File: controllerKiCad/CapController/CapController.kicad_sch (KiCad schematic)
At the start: 1 part

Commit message: Controller PCB Update
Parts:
- removed U?: Arduino_Nano, Arduino:Arduino_Nano, symbol Arduino:Arduino_Nano
- added 7_Seg_Dis_1, 7_Seg_Dis_2, 7_Seg_Dis_3: LTS-6960HR, Display_7Segment:7SegmentLED_LTS6760_LTS6780, symbol Display_Character:LTS-6960HR
- added Nano_33_IoT1: Arduino_Nano_33_IoT_Socket, arduino-library:Arduino_Nano_33_IoT_Socket, symbol arduino-library:Arduino_Nano_33_IoT_Socket
- added PMOD_Connector1: Conn_02x06_Counter_Clockwise, Connector_IDC:IDC-Header_2x06_P2.54mm_Horizontal, symbol Connector_Generic:Conn_02x06_Counter_Clockwise
- added Power_Terminal1: Screw_1x2, TerminalBlock:TerminalBlock_Altech_AK300-2_P5.00mm, symbol Connector:Screw_Terminal_01x02
- added SW_Car1, SW_Car2, SW_Car3, SW_Start1, SW_Stop_Reset1: SW_MEC_5E, symbol Switch:SW_MEC_5E
- added Shift_Reg_1, Shift_Reg_2, Shift_Reg_3: 74LS595, symbol 74xx:74LS595
- added Trigger_Pot1, Wheel_Pot1: Screw_1x3, TerminalBlock:TerminalBlock_Altech_AK300-3_P5.00mm, symbol Connector:Screw_Terminal_01x03
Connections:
- new net: Nano_33_IoT1.D8, Wheel_Pot1.2 (Pin_2)
- new net: Nano_33_IoT1.D13 (D13_SCK), SW_Car3.1
- new net: Nano_33_IoT1.D12 (D12_MISO), SW_Car2.1
- new net: Nano_33_IoT1.VIN, Power_Terminal1.2 (Pin_2)
- new net: 7_Seg_Dis_3.1 (e), Shift_Reg_3.4 (QE)
- new net: 7_Seg_Dis_3.10 (g), Shift_Reg_3.6 (QG)
- new net: 7_Seg_Dis_3.2 (d), Shift_Reg_3.3 (QD)
- new net: 7_Seg_Dis_3.4 (c), Shift_Reg_3.2 (QC)
- new net: 7_Seg_Dis_3.6 (b), Shift_Reg_3.1 (QB)
- new net: 7_Seg_Dis_3.7 (a), Shift_Reg_3.15 (QA)
- new net: 7_Seg_Dis_3.9 (f), Shift_Reg_3.5 (QF)
- new net: Nano_33_IoT1.D10, SW_Start1.1
- new net: 7_Seg_Dis_2.1 (e), Shift_Reg_2.4 (QE)
- new net: 7_Seg_Dis_2.10 (g), Shift_Reg_2.6 (QG)
- new net: 7_Seg_Dis_2.2 (d), Shift_Reg_2.3 (QD)
- new net: 7_Seg_Dis_2.4 (c), Shift_Reg_2.2 (QC)
- new net: 7_Seg_Dis_2.6 (b), Shift_Reg_2.1 (QB)
- new net: 7_Seg_Dis_2.7 (a), Shift_Reg_2.15 (QA)
- new net: 7_Seg_Dis_2.9 (f), Shift_Reg_2.5 (QF)
- new net: Nano_33_IoT1.A3, PMOD_Connector1.10 (Pin_10)
- new net: Nano_33_IoT1.A4 (A4/SDA), PMOD_Connector1.3 (Pin_3)
- new net: Nano_33_IoT1.A5 (A5/SCL), PMOD_Connector1.4 (Pin_4)
- new net: Nano_33_IoT1.A6, PMOD_Connector1.5 (Pin_5)
- new net: Nano_33_IoT1.A7, PMOD_Connector1.6 (Pin_6)
- new net: Nano_33_IoT1.A0 (A0/DAC), PMOD_Connector1.7 (Pin_7)
- new net: Nano_33_IoT1.A1, PMOD_Connector1.8 (Pin_8)
- new net: Nano_33_IoT1.A2, PMOD_Connector1.9 (Pin_9)
- new net: Shift_Reg_1.7 (QH), Shift_Reg_2.14 (SER)
- new net: Shift_Reg_2.7 (QH), Shift_Reg_3.14 (SER)
- new net: Nano_33_IoT1.D11 (D11_MOSI), SW_Car1.1
- new net: Nano_33_IoT1.D7, Trigger_Pot1.2 (Pin_2)
- new net: Nano_33_IoT1.D9, SW_Stop_Reset1.1
- new net: 7_Seg_Dis_1.6 (b), Shift_Reg_1.1 (QB)
- new net: 7_Seg_Dis_1.7 (a), Shift_Reg_1.15 (QA)
- new net: 7_Seg_Dis_1.4 (c), Shift_Reg_1.2 (QC)
- new net: 7_Seg_Dis_1.2 (d), Shift_Reg_1.3 (QD)
- new net: 7_Seg_Dis_1.1 (e), Shift_Reg_1.4 (QE)
- new net: 7_Seg_Dis_1.9 (f), Shift_Reg_1.5 (QF)
- new net: 7_Seg_Dis_1.10 (g), Shift_Reg_1.6 (QG)
- new net +5V: Nano_33_IoT1.3V3 (3.3V), PMOD_Connector1.1 (Pin_1), PMOD_Connector1.12 (Pin_12), Shift_Reg_1.10 (~{SRCLR}), Shift_Reg_1.16 (VCC), Shift_Reg_2.10 (~{SRCLR}), Shift_Reg_2.16 (VCC), Shift_Reg_3.10 (~{SRCLR}), Shift_Reg_3.16 (VCC), Trigger_Pot1.1 (Pin_1), Wheel_Pot1.1 (Pin_1)
- new net GND: 7_Seg_Dis_1.3 (C.A.), 7_Seg_Dis_1.8 (C.A.), 7_Seg_Dis_2.3 (C.A.), 7_Seg_Dis_2.8 (C.A.), 7_Seg_Dis_3.3 (C.A.), 7_Seg_Dis_3.8 (C.A.), Nano_33_IoT1.GND1 (GND), PMOD_Connector1.11 (Pin_11), PMOD_Connector1.2 (Pin_2), Power_Terminal1.1 (Pin_1), SW_Car1.4 (A), SW_Car2.4 (A), SW_Car3.4 (A), SW_Start1.4 (A), SW_Stop_Reset1.4 (A), Shift_Reg_1.13 (~{OE}), Shift_Reg_1.8 (GND), Shift_Reg_2.13 (~{OE}), Shift_Reg_2.8 (GND), Shift_Reg_3.13 (~{OE}), Shift_Reg_3.8 (GND), Trigger_Pot1.3 (Pin_3), Wheel_Pot1.3 (Pin_3)
- new net LED_Data_In: Nano_33_IoT1.D4, Shift_Reg_1.14 (SER)
- new net LED_Data_In_CLK: Nano_33_IoT1.D5, Shift_Reg_1.11 (SRCLK), Shift_Reg_2.11 (SRCLK), Shift_Reg_3.12 (RCLK)
- new net LED_Store_CLK: Nano_33_IoT1.D6, Shift_Reg_1.12 (RCLK)
- no-connect marks 0 -> 7
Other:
- removed sheet 7seg3

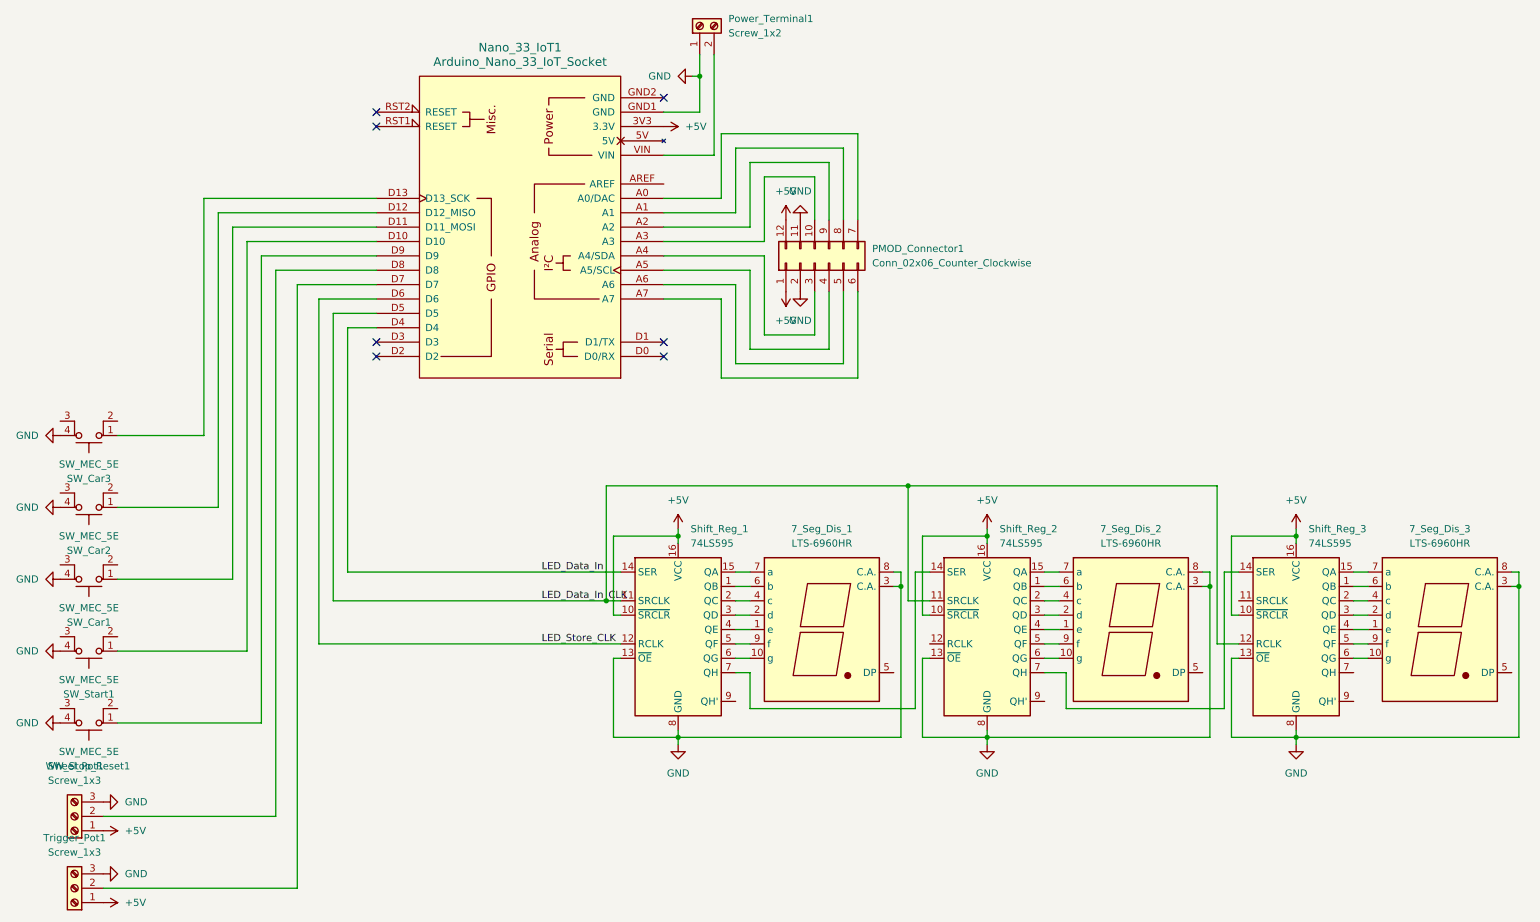
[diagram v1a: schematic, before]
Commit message: finished controller and added legacy veh code
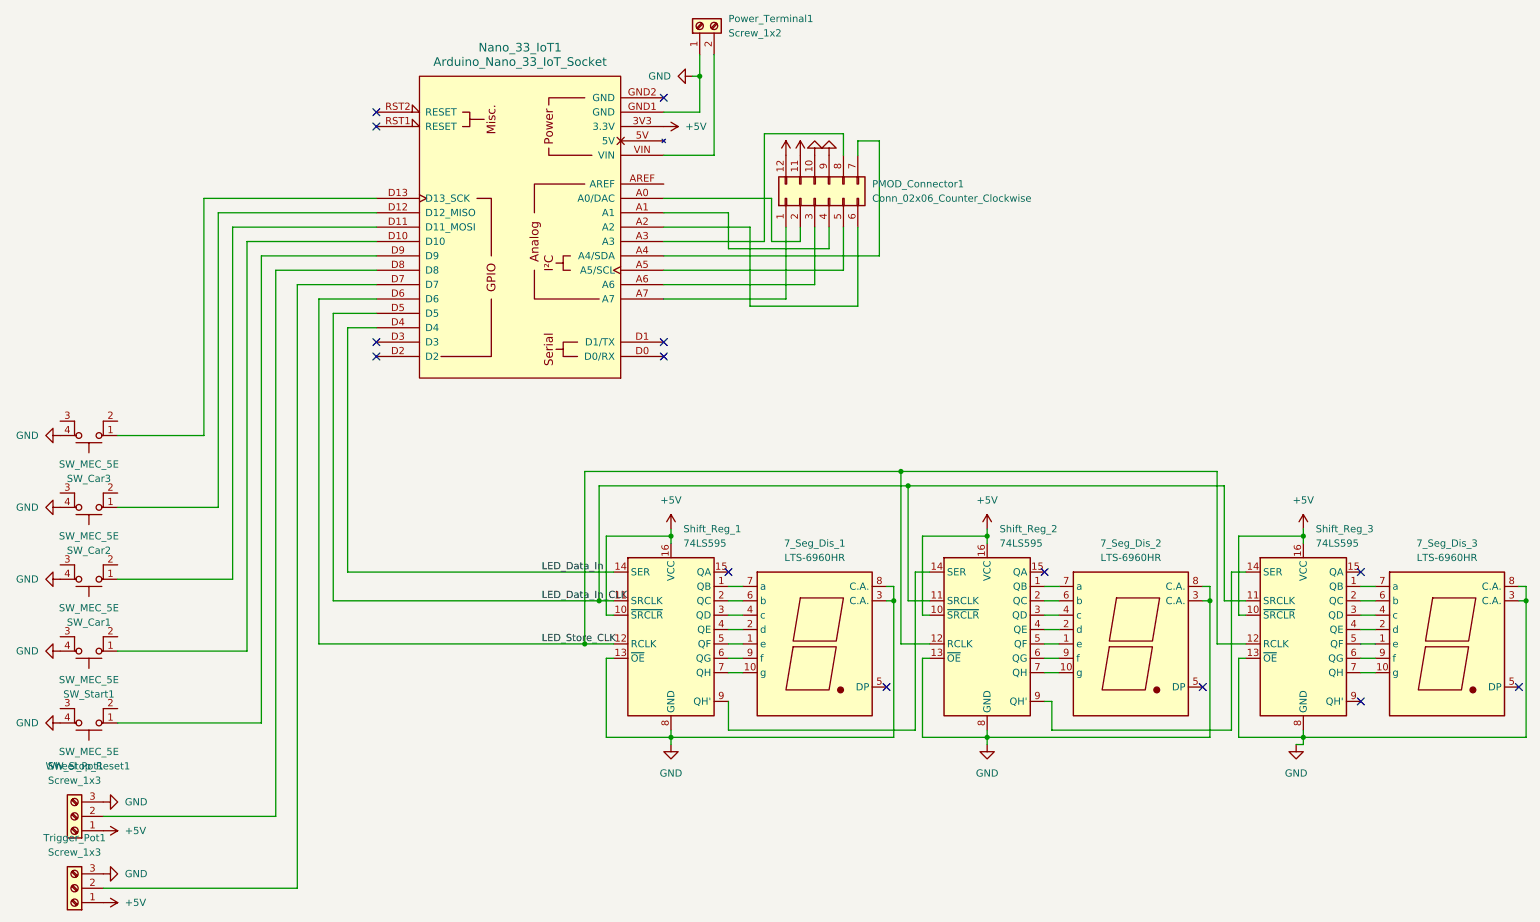
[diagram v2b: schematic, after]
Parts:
- SW_Car1, SW_Car2, SW_Car3, SW_Start1, SW_Stop_Reset1: footprint (none) -> Capstone:4Pin_Button
- Shift_Reg_1, Shift_Reg_2, Shift_Reg_3: footprint (none) -> Capstone:74HC595_16Pin_DIP
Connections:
- net +5V: now also PMOD_Connector1.11 (Pin_11); no longer PMOD_Connector1.1 (Pin_1)
- net GND: now also PMOD_Connector1.10 (Pin_10), PMOD_Connector1.9 (Pin_9); no longer PMOD_Connector1.11 (Pin_11), PMOD_Connector1.2 (Pin_2)
- net LED_Data_In_CLK: now also Shift_Reg_3.11 (SRCLK); no longer Shift_Reg_3.12 (RCLK)
- net LED_Store_CLK: now also Shift_Reg_2.12 (RCLK), Shift_Reg_3.12 (RCLK)
- net at 7_Seg_Dis_3.1 (e): now also Shift_Reg_3.5 (QF); no longer Shift_Reg_3.4 (QE)
- net at 7_Seg_Dis_3.10 (g): now also Shift_Reg_3.7 (QH); no longer Shift_Reg_3.6 (QG)
- net at 7_Seg_Dis_3.2 (d): now also Shift_Reg_3.4 (QE); no longer Shift_Reg_3.3 (QD)
- net at 7_Seg_Dis_3.4 (c): now also Shift_Reg_3.3 (QD); no longer Shift_Reg_3.2 (QC)
- net at 7_Seg_Dis_3.6 (b): now also Shift_Reg_3.2 (QC); no longer Shift_Reg_3.1 (QB)
- net at 7_Seg_Dis_3.7 (a): now also Shift_Reg_3.1 (QB); no longer Shift_Reg_3.15 (QA)
- net at 7_Seg_Dis_3.9 (f): now also Shift_Reg_3.6 (QG); no longer Shift_Reg_3.5 (QF)
- net at 7_Seg_Dis_2.1 (e): now also Shift_Reg_2.5 (QF); no longer Shift_Reg_2.4 (QE)
- net at 7_Seg_Dis_2.10 (g): now also Shift_Reg_2.7 (QH); no longer Shift_Reg_2.6 (QG)
- net at 7_Seg_Dis_2.2 (d): now also Shift_Reg_2.4 (QE); no longer Shift_Reg_2.3 (QD)
- net at 7_Seg_Dis_2.4 (c): now also Shift_Reg_2.3 (QD); no longer Shift_Reg_2.2 (QC)
- net at 7_Seg_Dis_2.6 (b): now also Shift_Reg_2.2 (QC); no longer Shift_Reg_2.1 (QB)
- net at 7_Seg_Dis_2.7 (a): now also Shift_Reg_2.1 (QB); no longer Shift_Reg_2.15 (QA)
- net at 7_Seg_Dis_2.9 (f): now also Shift_Reg_2.6 (QG); no longer Shift_Reg_2.5 (QF)
- net at Nano_33_IoT1.A3: now also PMOD_Connector1.8 (Pin_8); no longer PMOD_Connector1.10 (Pin_10)
- net at PMOD_Connector1.3 (Pin_3): now also Nano_33_IoT1.A6; no longer Nano_33_IoT1.A4 (A4/SDA)
- net at PMOD_Connector1.4 (Pin_4): now also Nano_33_IoT1.A1; no longer Nano_33_IoT1.A5 (A5/SCL)
- net at PMOD_Connector1.5 (Pin_5): now also Nano_33_IoT1.A5 (A5/SCL); no longer Nano_33_IoT1.A6
- net at Nano_33_IoT1.A7: now also PMOD_Connector1.1 (Pin_1); no longer PMOD_Connector1.6 (Pin_6)
- net at Nano_33_IoT1.A0 (A0/DAC): now also PMOD_Connector1.2 (Pin_2); no longer PMOD_Connector1.7 (Pin_7)
- net at Nano_33_IoT1.A2: now also PMOD_Connector1.6 (Pin_6); no longer PMOD_Connector1.9 (Pin_9)
- net at Shift_Reg_2.14 (SER): now also Shift_Reg_1.9 (QH'); no longer Shift_Reg_1.7 (QH)
- net at Shift_Reg_3.14 (SER): now also Shift_Reg_2.9 (QH'); no longer Shift_Reg_2.7 (QH)
- net at Shift_Reg_1.1 (QB): now also 7_Seg_Dis_1.7 (a); no longer 7_Seg_Dis_1.6 (b)
- net at Shift_Reg_1.15 (QA): no longer 7_Seg_Dis_1.7 (a)
- net at Shift_Reg_1.2 (QC): now also 7_Seg_Dis_1.6 (b); no longer 7_Seg_Dis_1.4 (c)
- net at Shift_Reg_1.3 (QD): now also 7_Seg_Dis_1.4 (c); no longer 7_Seg_Dis_1.2 (d)
- net at Shift_Reg_1.4 (QE): now also 7_Seg_Dis_1.2 (d); no longer 7_Seg_Dis_1.1 (e)
- net at Shift_Reg_1.5 (QF): now also 7_Seg_Dis_1.1 (e); no longer 7_Seg_Dis_1.9 (f)
- net at Shift_Reg_1.6 (QG): now also 7_Seg_Dis_1.9 (f); no longer 7_Seg_Dis_1.10 (g)
- new net: Nano_33_IoT1.A4 (A4/SDA), PMOD_Connector1.7 (Pin_7)
- new net: 7_Seg_Dis_1.10 (g), Shift_Reg_1.7 (QH)
- no-connect marks 7 -> 14
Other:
- moved on the sheet: 7_Seg_Dis_1, 7_Seg_Dis_2, 7_Seg_Dis_3, PMOD_Connector1, Shift_Reg_1, Shift_Reg_3

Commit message: updated controller kicad files
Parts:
- added R1, R10, R11, R12, R13, R14, R15, R16, R17, R18, R19, R2, R20, R21, R3, R4, R5, R6, R7, R8, R9: R, Resistor_THT:R_Axial_DIN0309_L9.0mm_D3.2mm_P12.70mm_Horizontal, symbol Device:R
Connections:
- net at 7_Seg_Dis_3.1 (e): now also R19.1; no longer Shift_Reg_3.5 (QF)
- net at 7_Seg_Dis_3.10 (g): now also R21.1; no longer Shift_Reg_3.7 (QH)
- net at 7_Seg_Dis_3.2 (d): now also R18.1; no longer Shift_Reg_3.4 (QE)
- net at 7_Seg_Dis_3.4 (c): now also R17.1; no longer Shift_Reg_3.3 (QD)
- net at 7_Seg_Dis_3.6 (b): now also R16.1; no longer Shift_Reg_3.2 (QC)
- net at 7_Seg_Dis_3.7 (a): now also R15.1; no longer Shift_Reg_3.1 (QB)
- net at 7_Seg_Dis_3.9 (f): now also R20.1; no longer Shift_Reg_3.6 (QG)
- net at 7_Seg_Dis_2.1 (e): now also R12.1; no longer Shift_Reg_2.5 (QF)
- net at 7_Seg_Dis_2.10 (g): now also R14.1; no longer Shift_Reg_2.7 (QH)
- net at 7_Seg_Dis_2.2 (d): now also R11.1; no longer Shift_Reg_2.4 (QE)
- net at 7_Seg_Dis_2.4 (c): now also R10.1; no longer Shift_Reg_2.3 (QD)
- net at 7_Seg_Dis_2.6 (b): now also R9.1; no longer Shift_Reg_2.2 (QC)
- net at 7_Seg_Dis_2.7 (a): now also R8.1; no longer Shift_Reg_2.1 (QB)
- net at 7_Seg_Dis_2.9 (f): now also R13.1; no longer Shift_Reg_2.6 (QG)
- net at Shift_Reg_1.1 (QB): now also R1.2; no longer 7_Seg_Dis_1.7 (a)
- net at 7_Seg_Dis_1.6 (b): now also R2.1; no longer Shift_Reg_1.2 (QC)
- net at 7_Seg_Dis_1.4 (c): now also R3.1; no longer Shift_Reg_1.3 (QD)
- net at Shift_Reg_1.4 (QE): now also R4.2; no longer 7_Seg_Dis_1.2 (d)
- net at 7_Seg_Dis_1.1 (e): now also R5.1; no longer Shift_Reg_1.5 (QF)
- net at 7_Seg_Dis_1.9 (f): now also R6.1; no longer Shift_Reg_1.6 (QG)
- net at Shift_Reg_1.7 (QH): now also R7.2; no longer 7_Seg_Dis_1.10 (g)
- new net: R13.2, Shift_Reg_2.6 (QG)
- new net: R19.2, Shift_Reg_3.5 (QF)
- new net: R6.2, Shift_Reg_1.6 (QG)
- new net: R10.2, Shift_Reg_2.3 (QD)
- new net: R14.2, Shift_Reg_2.7 (QH)
- new net: R5.2, Shift_Reg_1.5 (QF)
- new net: R8.2, Shift_Reg_2.1 (QB)
- new net: R9.2, Shift_Reg_2.2 (QC)
- new net: R11.2, Shift_Reg_2.4 (QE)
- new net: R12.2, Shift_Reg_2.5 (QF)
- new net: R20.2, Shift_Reg_3.6 (QG)
- new net: R3.2, Shift_Reg_1.3 (QD)
- new net: R15.2, Shift_Reg_3.1 (QB)
- new net: R16.2, Shift_Reg_3.2 (QC)
- new net: R17.2, Shift_Reg_3.3 (QD)
- new net: R18.2, Shift_Reg_3.4 (QE)
- new net: R21.2, Shift_Reg_3.7 (QH)
- new net: R2.2, Shift_Reg_1.2 (QC)
- new net: 7_Seg_Dis_1.10 (g), R7.1
- new net: 7_Seg_Dis_1.2 (d), R4.1
- new net: 7_Seg_Dis_1.7 (a), R1.1
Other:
- moved on the sheet: 7_Seg_Dis_1, 7_Seg_Dis_2, 7_Seg_Dis_3, Shift_Reg_1, Shift_Reg_2, Shift_Reg_3
